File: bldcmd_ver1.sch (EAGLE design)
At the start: 46 parts, among them IC1 STSPIN32F0, IC2 AS5047P-ATSM, IC3 ADM4852ACPZ-REEL7, J1 DF65-3P-1.7V(21), Q1 PSMN2R4-30MLD, Q2 PSMN2R4-30MLD, Q3 PSMN2R4-30MLD, Q4 PSMN2R4-30MLD, Q5 PSMN2R4-30MLD, Q6 PSMN2R4-30MLD

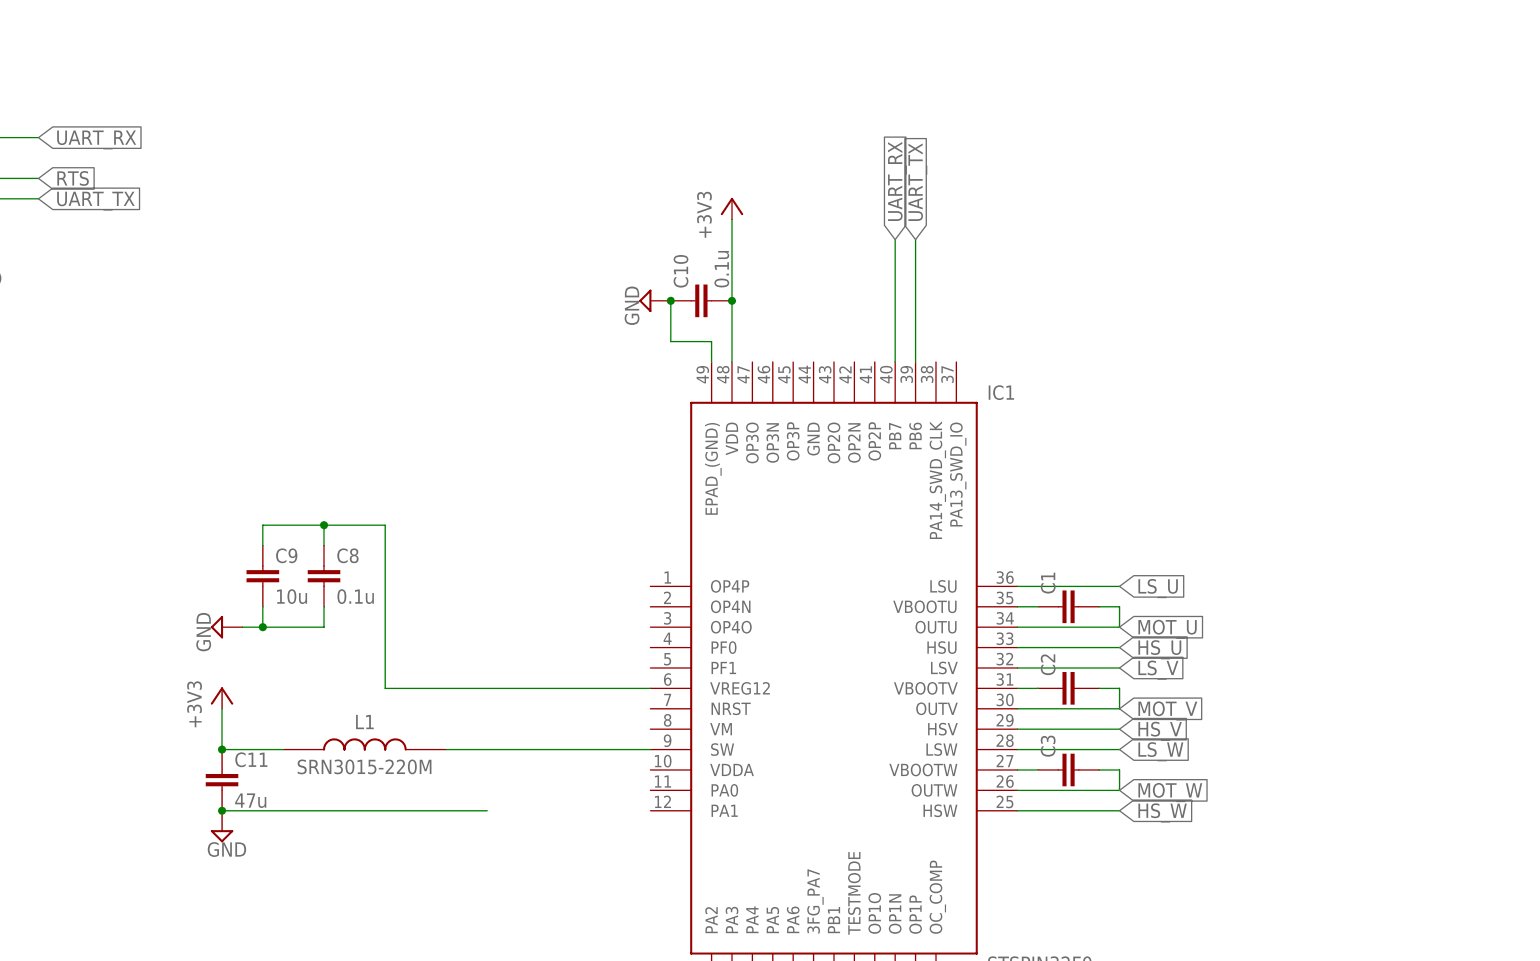
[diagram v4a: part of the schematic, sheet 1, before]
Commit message: ブリッジ回路AW攻めた
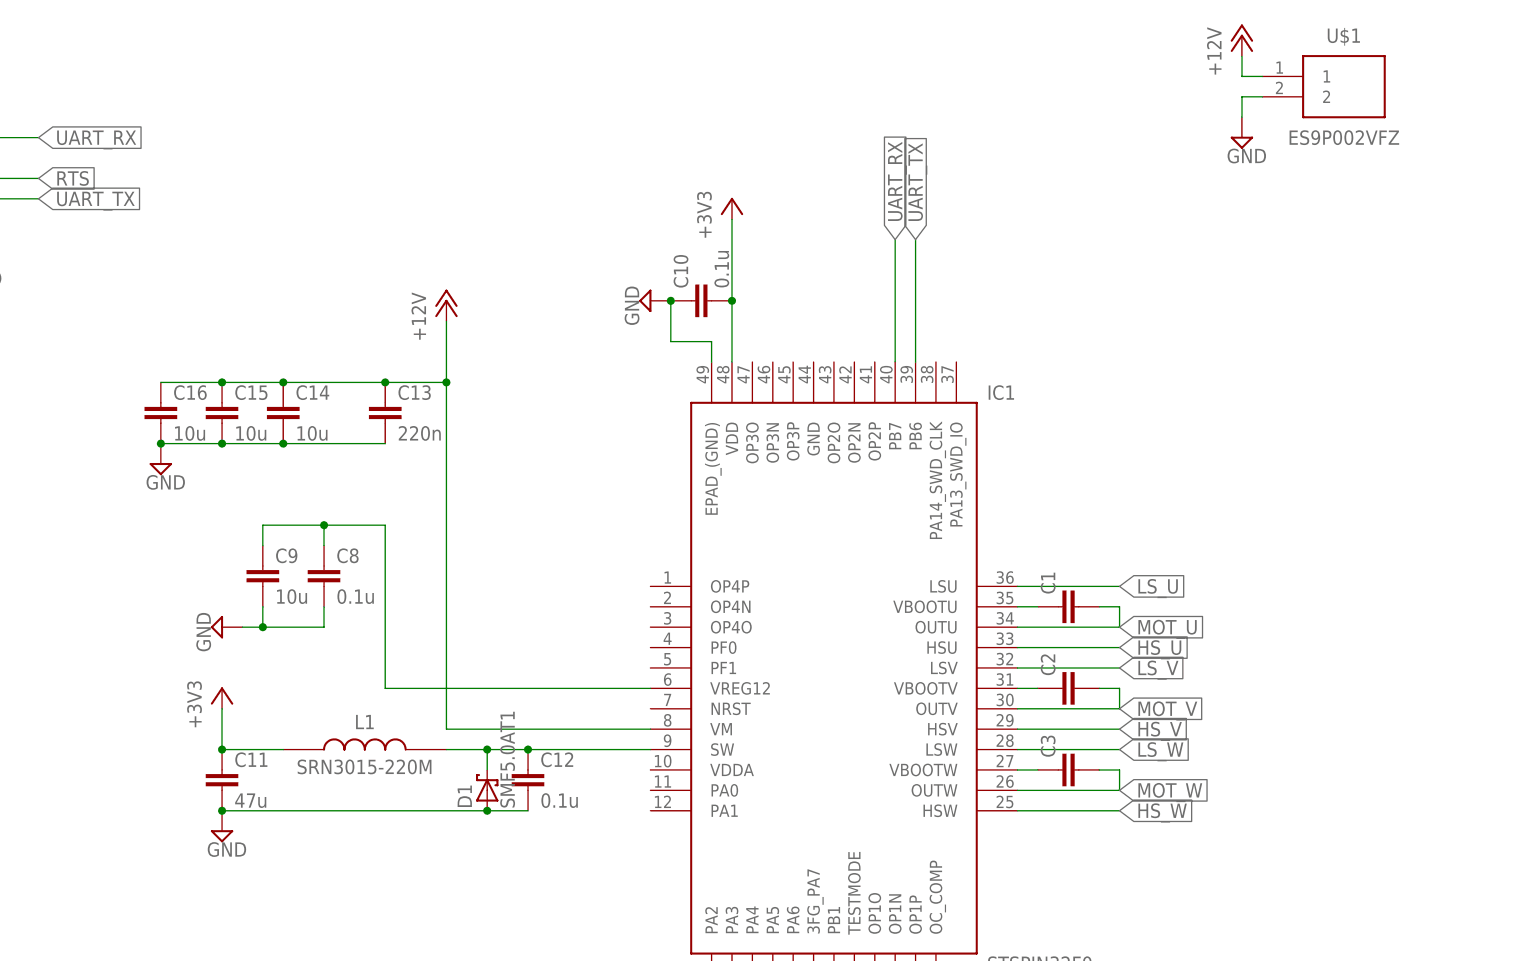
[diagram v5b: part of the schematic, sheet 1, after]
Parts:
- added C12: 0.1u, rcl:C-EUC0603K
- added C13: 220n, rcl:C-EUC0805K
- added C14, C15, C16: 10u, rcl:C-EUC3225
- added D1: SMF5.0AT1, diode:SMF5.0AT1
- added U$1: ES9P002VFZ, rcssl_lib:ES9P002VFZ
- TP1, TP2, TP3, TP4, TP5, TP6, TP7: value TPTP06R -> TPTP08R; device testpad:TPTP06R -> testpad:TPTP08R
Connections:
- removed net N$10: C4.1, C5.1, C6.1, Q1.D, Q3.D, Q5.D
- new net +12V: C13.1, C14.1, C15.1, C16.1, C4.1, C5.1, C6.1, IC1.VM, Q1.D, Q3.D, Q5.D, U$1.1
- net GND: now also C12.2, C13.2, C14.2, C15.2, C16.2, D1.A, U$1.2
- net MOT_U: now also J1.3; no longer J1.1
- net MOT_W: now also J1.1; no longer J1.3
- net N$18: now also C12.1, D1.C
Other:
- moved on the sheet: J1

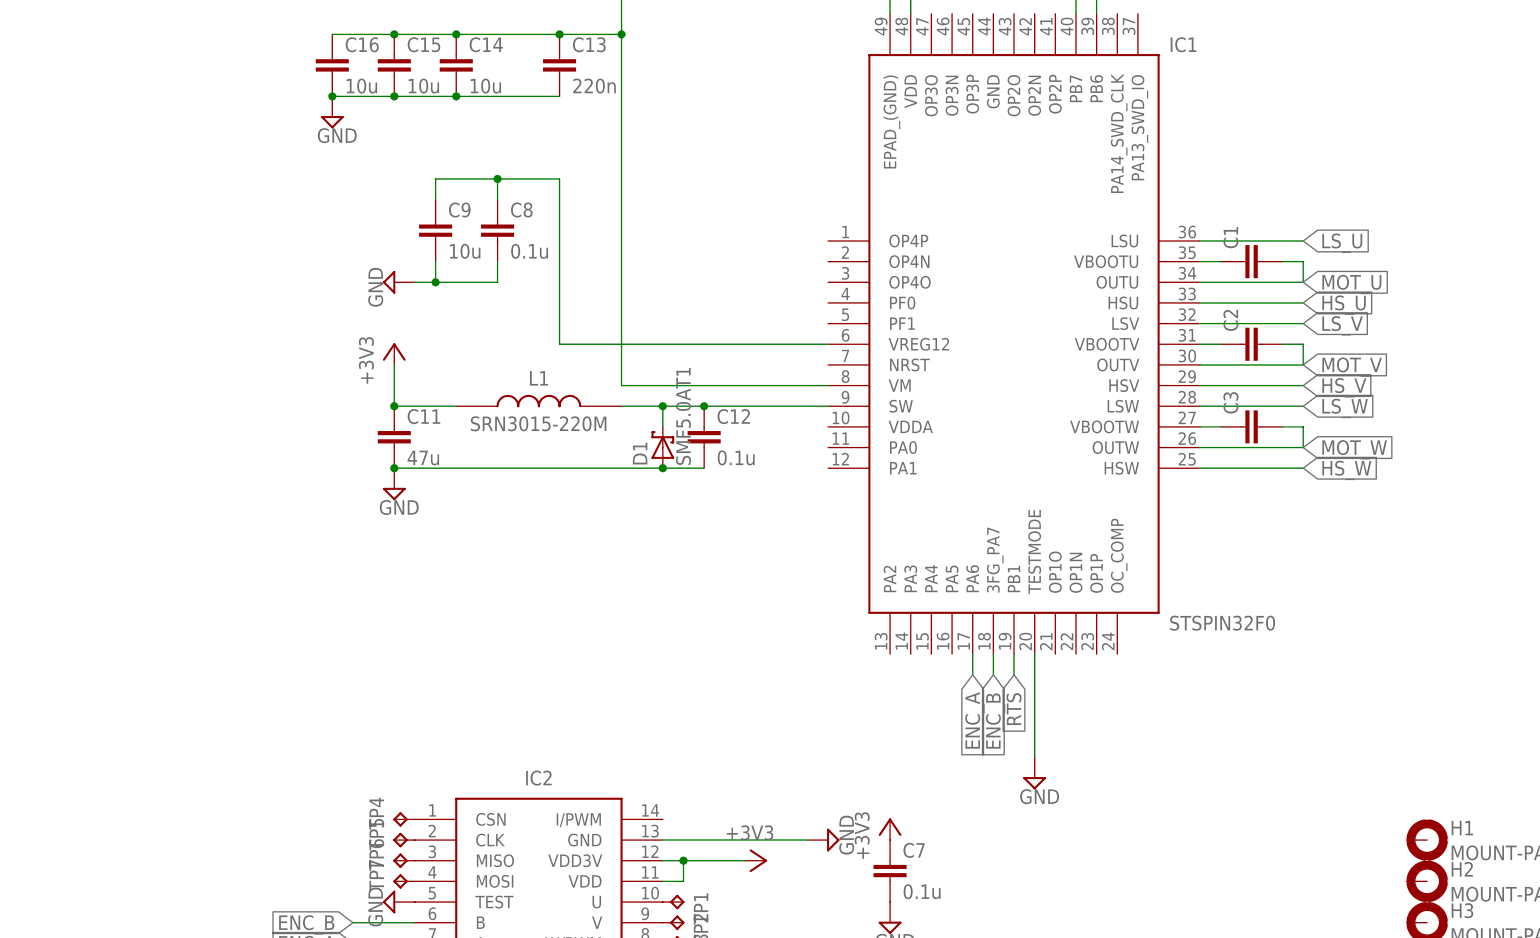
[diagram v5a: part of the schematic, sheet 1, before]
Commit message: 現状乗っている部品はほぼ配線完了
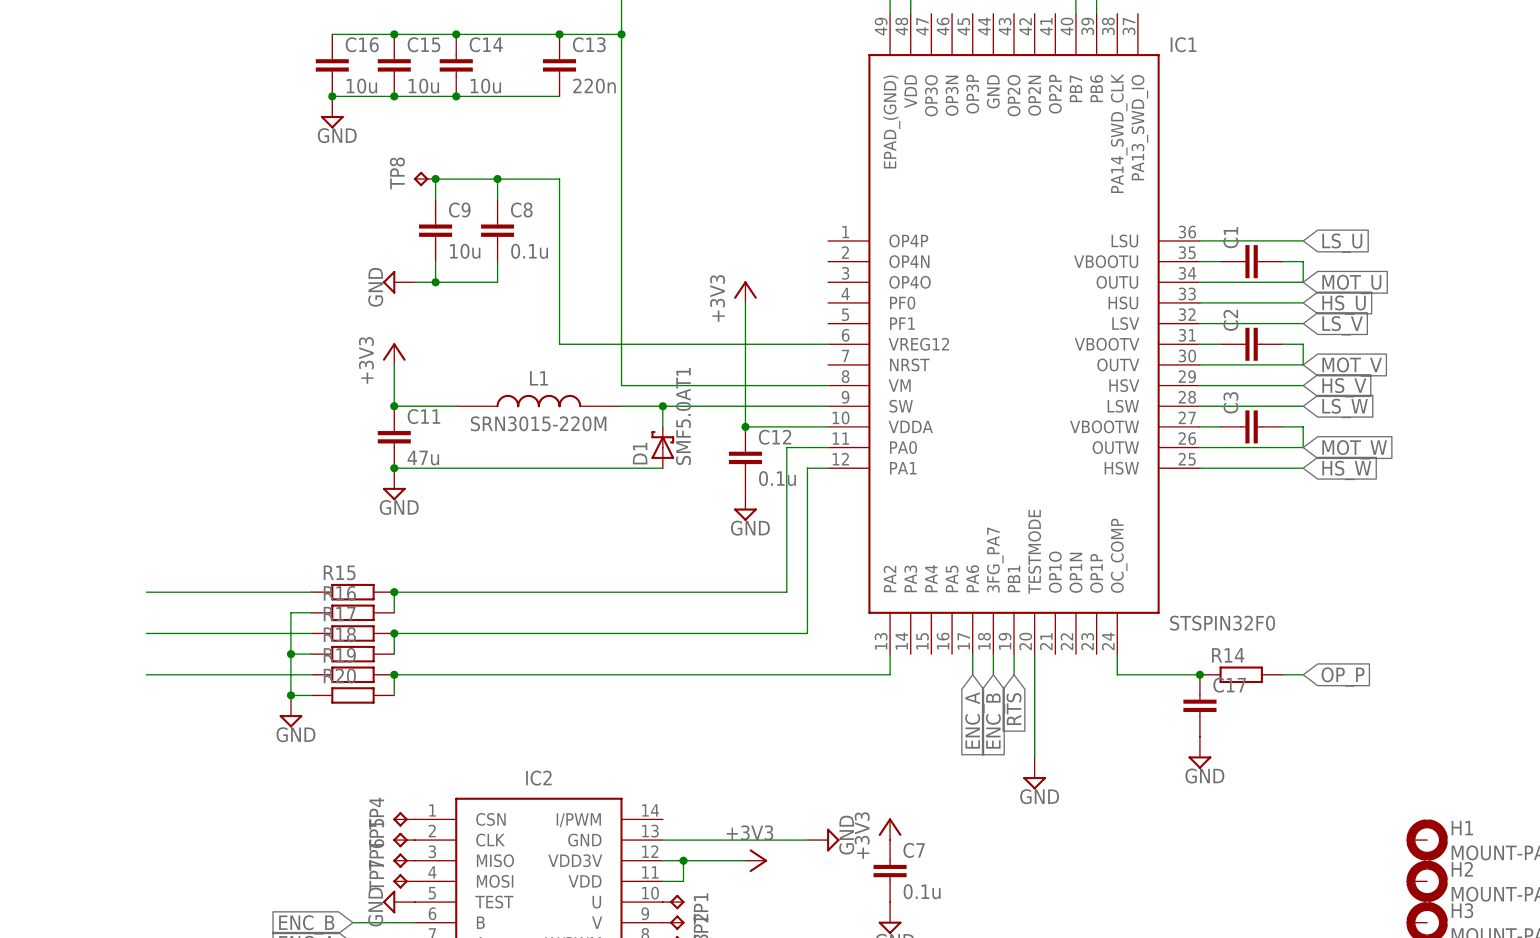
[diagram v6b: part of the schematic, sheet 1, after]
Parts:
- added C17: (no value), rcl:C-EUC0402
- added R14, R15, R16, R17, R18, R19, R20: (no value), rcl:R-EU_R0402
- added TP8: TPPAD1-13, testpad:TPPAD1-13
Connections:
- new net N$10: C17.1, IC1.OC_COMP, R14.1
- new net N$20: IC1.PA0, R15.2, R16.2
- new net N$21: IC1.PA1, R17.2, R18.2
- new net N$22: IC1.PA2, R19.2, R20.2
- new net N$23: R19.1
- new net N$24: R17.1
- new net N$25: R15.1
- net +3V3: now also C12.1, IC1.VDDA
- net GND: now also C17.2, R16.1, R18.1, R20.1
- net N$18: no longer C12.1
- net N$19: now also TP8.TP
- net OP_P: now also R14.2
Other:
- moved on the sheet: C12
